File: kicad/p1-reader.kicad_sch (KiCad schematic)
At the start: 10 parts, among them J1 RJ12, J2 ESP32 left, J3 ESP32 right, U1 4N35

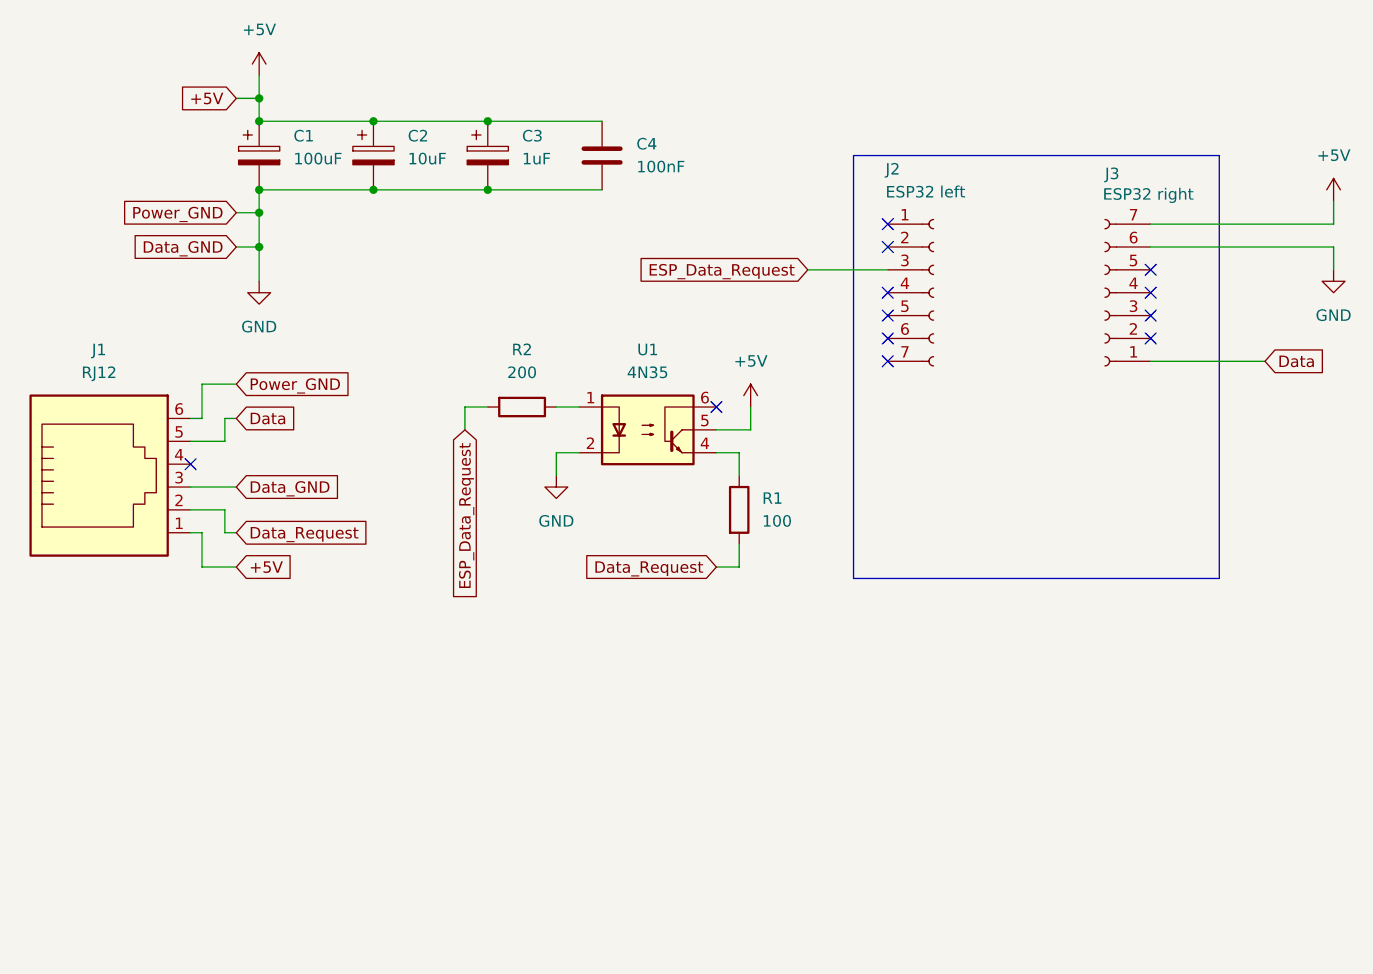
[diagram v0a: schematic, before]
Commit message: Add status LED
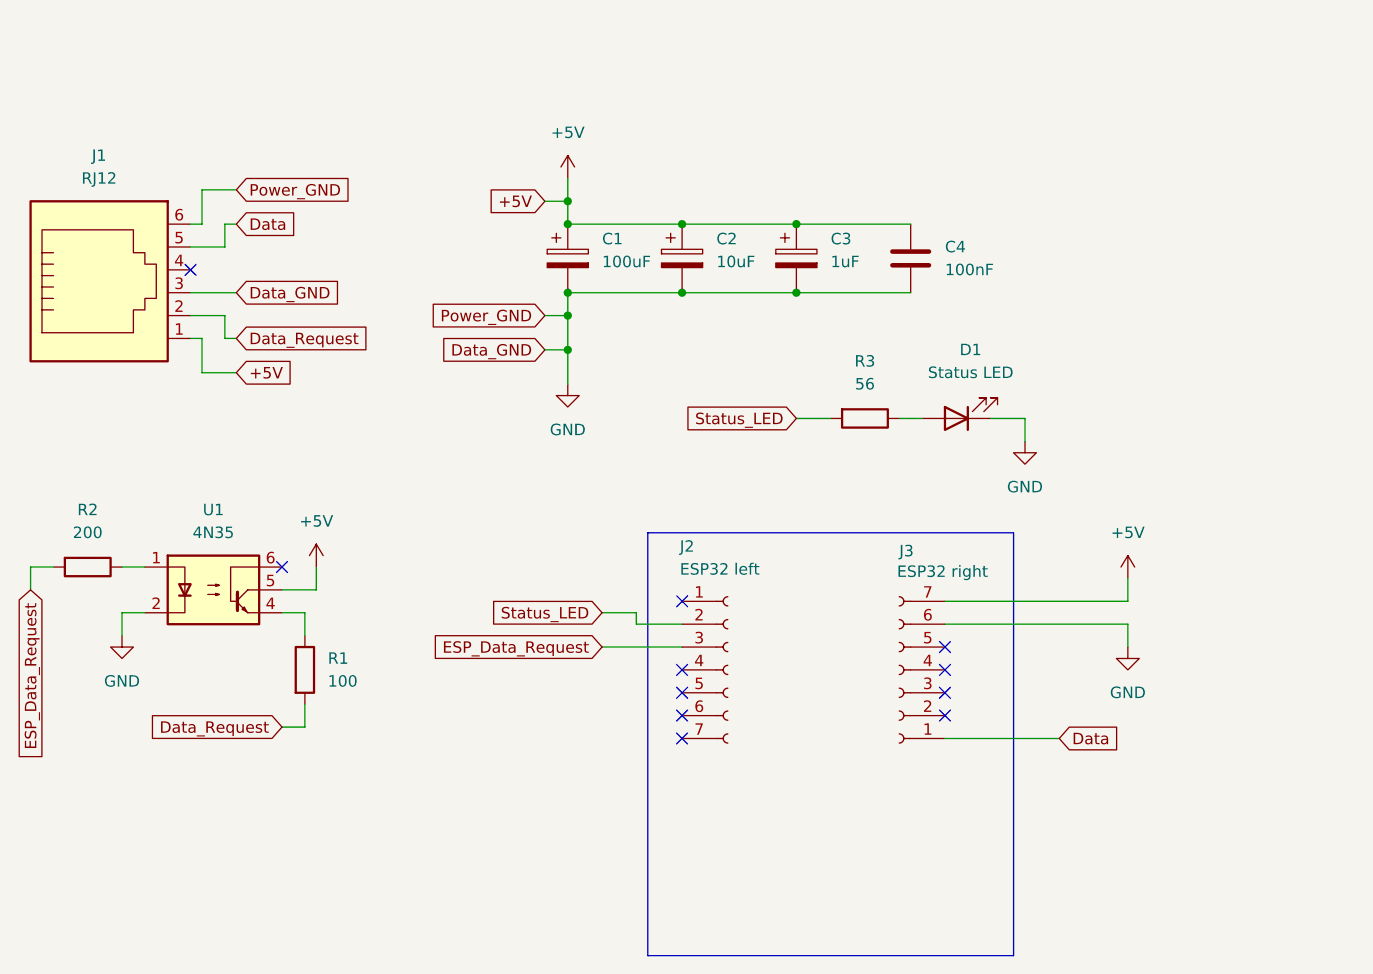
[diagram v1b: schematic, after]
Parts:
- added D1: Status LED, LED_THT:LED_D3.0mm, symbol Device:LED
- added R3: 56, Resistor_THT:R_Axial_DIN0207_L6.3mm_D2.5mm_P10.16mm_Horizontal, symbol Device:R
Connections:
- net GND: now also D1.1 (K)
- net Status_LED: now reaches J2.2 (Pin_2)
- net Status_LED: now also R3.2
- new net: D1.2 (A), R3.1
- no-connect marks 12 -> 11
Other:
- moved on the sheet: C1, C2, C3, C4, J1, J2, J3, R1, R2, U1

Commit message: Update for Stoen
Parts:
- added R4: 1K, symbol Device:R
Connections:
- net Data: now also R4.2
- net +3V3: now reaches J3.5 (Pin_5)
- net +3V3: now also R4.1
- no-connect marks 11 -> 10
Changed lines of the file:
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@@
 	)
 	(junction
+		(at 204.47 116.84)
+		(diameter 0)
+		(color 0 0 0 0)
+	)
+	(junction
 		(at 175.26 67.31)
 		(diameter 0)
@@
 	)
 	(junction
+		(at 204.47 106.68)
+		(diameter 0)
+		(color 0 0 0 0)
+	)
+	(junction
 		(at 162.56 59.69)
 		(diameter 0)
@@
 	)
 	(no_connect
-		(at 191.77 106.68)
-	)
-	(no_connect
 		(at 162.56 109.22)
 	)
@@
 	(wire
 		(pts
+			(xy 204.47 116.84) (xy 204.47 115.57)
+		)
+		(stroke
+			(width 0)
+			(type default)
+		)
+	)
+	(wire
+		(pts
 			(xy 149.86 69.85) (xy 147.32 69.85)
 		)
@@
 	(wire
 		(pts
-			(xy 212.09 104.14) (xy 212.09 106.68)
+			(xy 218.44 104.14) (xy 218.44 106.68)
+		)
+		(stroke
+			(width 0)
+			(type default)
+		)
+	)
+	(wire
+		(pts
+			(xy 191.77 106.68) (xy 204.47 106.68)
 		)
 		(stroke
@@
 	(wire
 		(pts
-			(xy 191.77 104.14) (xy 212.09 104.14)
+			(xy 204.47 116.84) (xy 209.55 116.84)
+		)
+		(stroke
+			(width 0)
+			(type default)
+		)
+	)
+	(wire
+		(pts
+			(xy 204.47 106.68) (xy 204.47 99.06)
 		)
 		(stroke
@@
 	(wire
 		(pts
+			(xy 191.77 104.14) (xy 218.44 104.14)
+		)
+		(stroke
+			(width 0)
+			(type default)
+		)
+	)
+	(wire
+		(pts
 			(xy 111.76 62.23) (xy 107.95 62.23)
 		)
@@
 	(wire
 		(pts
-			(xy 191.77 101.6) (xy 212.09 101.6)
+			(xy 191.77 101.6) (xy 218.44 101.6)
 		)
 		(stroke
@@
 	(wire
 		(pts
-			(xy 212.09 101.6) (xy 212.09 99.06)
+			(xy 218.44 101.6) (xy 218.44 99.06)
+		)
+		(stroke
+			(width 0)
+			(type default)
+		)
+	)
+	(wire
+		(pts
+			(xy 204.47 106.68) (xy 204.47 107.95)
 		)
 		(stroke
@@
 	(global_label "Data"
 		(shape input)
-		(at 204.47 116.84 0)
+		(at 209.55 116.84 0)
 		(fields_autoplaced yes)
 		(effects
@@
 		)
 		(property "Intersheetrefs" "${INTERSHEET_REFS}"
-			(at 211.7489 116.84 0)
+			(at 216.8289 116.84 0)
 			(effects
 				(font
@@
 	(symbol
 		(lib_id "power:+5V")
-		(at 212.09 99.06 0)
+		(at 218.44 99.06 0)
 		(unit 1)
 		(exclude_from_sim no)
@@
 		(fields_autoplaced yes)
 		(property "Reference" "#PWR05"
-			(at 212.09 102.87 0)
+			(at 218.44 102.87 0)
 			(effects
 				(font
@@
 		)
 		(property "Value" "+5V"
-			(at 212.09 93.98 0)
+			(at 218.44 93.98 0)
 			(effects
 				(font
@@
 		)
 		(property "Footprint" ""
-			(at 212.09 99.06 0)
+			(at 218.44 99.06 0)
 			(effects
 				(font
@@
 		)
 		(property "Datasheet" ""
-			(at 212.09 99.06 0)
+			(at 218.44 99.06 0)
 			(effects
 				(font
@@
 		)
 		(property "Description" "Power symbol creates a global label with name \"+5V\""
-			(at 212.09 99.06 0)
+			(at 218.44 99.06 0)
 			(effects
 				(font
@@
 	)
 	(symbol
+		(lib_id "power:+5V")
+		(at 204.47 99.06 0)
+		(unit 1)
+		(exclude_from_sim no)
+		(in_bom yes)
+		(on_board yes)
+		(dnp no)
+		(fields_autoplaced yes)
+		(property "Reference" "#PWR08"
+			(at 204.47 102.87 0)
+			(effects
+				(font
+					(size 1.27 1.27)
+				)
+				(hide yes)
+			)
+		)
+		(property "Value" "+3V3"
+			(at 204.47 93.98 0)
+			(effects
+				(font
+					(size 1.27 1.27)
+				)
+			)
+		)
+		(property "Footprint" ""
+			(at 204.47 99.06 0)
+			(effects
+				(font
+					(size 1.27 1.27)
+				)
+				(hide yes)
+			)
+		)
+		(property "Datasheet" ""
+			(at 204.47 99.06 0)
+			(effects
+				(font
+					(size 1.27 1.27)
+				)
+				(hide yes)
+			)
+		)
+		(property "Description" "Power symbol creates a global label with name \"+5V\""
+			(at 204.47 99.06 0)
+			(effects
+				(font
+					(size 1.27 1.27)
+				)
+				(hide yes)
+			)
+		)
+		(pin "1"
+		)
+		(instances
+			(project "p1-reader"
+				(path "/f299598e-d2e1-4c04-87e1-3c0f09a575af"
+					(reference "#PWR08")
+					(unit 1)
+				)
+			)
+		)
+	)
+	(symbol
 		(lib_id "Device:R")
 		(at 182.88 81.28 270)
@@
 	)
 	(symbol
+		(lib_id "Device:R")
+		(at 204.47 111.76 0)
+		(unit 1)
+		(exclude_from_sim no)
+		(in_bom yes)
+		(on_board yes)
+		(dnp no)
+		(fields_autoplaced yes)
+		(property "Reference" "R4"
+			(at 207.01 110.4899 0)
+			(effects
+				(font
+					(size 1.27 1.27)
+				)
+				(justify left)
+			)
+		)
+		(property "Value" "1K"
+			(at 207.01 113.0299 0)
+			(effects
+				(font
+					(size 1.27 1.27)
+				)
+				(justify left)
+			)
+		)
+		(property "Footprint" ""
+			(at 202.692 111.76 90)
+			(effects
+				(font
+					(size 1.27 1.27)
+				)
+				(hide yes)
+			)
+		)
+		(property "Datasheet" "~"
+			(at 204.47 111.76 0)
+			(effects
+				(font
+					(size 1.27 1.27)
+				)
+				(hide yes)
+			)
+		)
+		(property "Description" "Resistor"
+			(at 204.47 111.76 0)
+			(effects
+				(font
+					(size 1.27 1.27)
+				)
+				(hide yes)
+			)
+		)
+		(pin "2"
+		)
+		(pin "1"
+		)
+		(instances
+			(project ""
+				(path "/f299598e-d2e1-4c04-87e1-3c0f09a575af"
+					(reference "R4")
+					(unit 1)
+				)
+			)
+		)
+	)
+	(symbol
 		(lib_id "Device:C_Polarized")
 		(at 175.26 63.5 0)
@@
 	(symbol
 		(lib_id "power:GND")
-		(at 212.09 106.68 0)
+		(at 218.44 106.68 0)
 		(unit 1)
 		(exclude_from_sim no)
@@
 		(fields_autoplaced yes)
 		(property "Reference" "#PWR06"
-			(at 212.09 113.03 0)
+			(at 218.44 113.03 0)
 			(effects
 				(font
@@
 		)
 		(property "Value" "GND"
-			(at 212.09 111.76 0)
+			(at 218.44 111.76 0)
 			(effects
 				(font
@@
 		)
 		(property "Footprint" ""
-			(at 212.09 106.68 0)
+			(at 218.44 106.68 0)
 			(effects
 				(font
@@
 		)
 		(property "Datasheet" ""
-			(at 212.09 106.68 0)
+			(at 218.44 106.68 0)
 			(effects
 				(font
@@
 		)
 		(property "Description" "Power symbol creates a global label with name \"GND\" , ground"
-			(at 212.09 106.68 0)
+			(at 218.44 106.68 0)
 			(effects
 				(font
